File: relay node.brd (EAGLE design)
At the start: 67.8 x 40.6 mm, 25 parts, among them J1 Channels, J2 LED, J3 PROG, J4 AUX, U1 ESP-WROOM-02U, U2 MCP23018-E/SS, U5 TLV75533

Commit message: Minor changes
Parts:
- renumbered U5 to U3
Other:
- board text added: "RELAY NODE REV 1.1a"
- board text added: "RELAY NODE Rev 1.1a"
- board text removed: "SFM RELAY NODE REV 1.1a"
- board text removed: "SFM RELAY NODE Rev 1.1a"
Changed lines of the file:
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@@
 <grid distance="0.127" unitdist="mm" unit="mm" style="lines" multiple="1" display="yes" altdistance="0.0127" altunitdist="mm" altunit="mm"/>
 <layers>
-<layer number="1" name="Top" color="4" fill="1" visible="yes" active="yes"/>
+<layer number="1" name="Top" color="4" fill="1" visible="no" active="yes"/>
 <layer number="16" name="Bottom" color="1" fill="1" visible="yes" active="yes"/>
-<layer number="17" name="Pads" color="2" fill="1" visible="yes" active="yes"/>
-<layer number="18" name="Vias" color="2" fill="1" visible="yes" active="yes"/>
-<layer number="19" name="Unrouted" color="6" fill="1" visible="yes" active="yes"/>
-<layer number="20" name="Dimension" color="24" fill="1" visible="yes" active="yes"/>
-<layer number="21" name="tPlace" color="7" fill="1" visible="yes" active="yes"/>
-<layer number="22" name="bPlace" color="7" fill="1" visible="yes" active="yes"/>
-<layer number="23" name="tOrigins" color="15" fill="1" visible="yes" active="yes"/>
-<layer number="24" name="bOrigins" color="15" fill="1" visible="yes" active="yes"/>
-<layer number="25" name="tNames" color="7" fill="1" visible="yes" active="yes"/>
-<layer number="26" name="bNames" color="7" fill="1" visible="yes" active="yes"/>
+<layer number="17" name="Pads" color="2" fill="1" visible="no" active="yes"/>
+<layer number="18" name="Vias" color="2" fill="1" visible="no" active="yes"/>
+<layer number="19" name="Unrouted" color="6" fill="1" visible="no" active="yes"/>
+<layer number="20" name="Dimension" color="24" fill="1" visible="no" active="yes"/>
+<layer number="21" name="tPlace" color="7" fill="1" visible="no" active="yes"/>
+<layer number="22" name="bPlace" color="7" fill="1" visible="no" active="yes"/>
+<layer number="23" name="tOrigins" color="15" fill="1" visible="no" active="yes"/>
+<layer number="24" name="bOrigins" color="15" fill="1" visible="no" active="yes"/>
+<layer number="25" name="tNames" color="7" fill="1" visible="no" active="yes"/>
+<layer number="26" name="bNames" color="7" fill="1" visible="no" active="yes"/>
 <layer number="27" name="tValues" color="7" fill="1" visible="no" active="yes"/>
 <layer number="28" name="bValues" color="7" fill="1" visible="no" active="yes"/>
@@
 <layer number="37" name="tTest" color="7" fill="1" visible="no" active="yes"/>
 <layer number="38" name="bTest" color="7" fill="1" visible="no" active="yes"/>
-<layer number="39" name="tKeepout" color="4" fill="11" visible="yes" active="yes"/>
-<layer number="40" name="bKeepout" color="1" fill="11" visible="yes" active="yes"/>
-<layer number="41" name="tRestrict" color="4" fill="10" visible="yes" active="yes"/>
+<layer number="39" name="tKeepout" color="4" fill="11" visible="no" active="yes"/>
+<layer number="40" name="bKeepout" color="1" fill="11" visible="no" active="yes"/>
+<layer number="41" name="tRestrict" color="4" fill="10" visible="no" active="yes"/>
 <layer number="42" name="bRestrict" color="1" fill="10" visible="yes" active="yes"/>
 <layer number="43" name="vRestrict" color="2" fill="10" visible="no" active="yes"/>
@@
 <layer number="49" name="Reference" color="7" fill="1" visible="no" active="yes"/>
 <layer number="50" name="dxf" color="7" fill="1" visible="no" active="yes"/>
-<layer number="51" name="tDocu" color="7" fill="1" visible="yes" active="yes"/>
-<layer number="52" name="bDocu" color="7" fill="1" visible="yes" active="yes"/>
+<layer number="51" name="tDocu" color="7" fill="1" visible="no" active="yes"/>
+<layer number="52" name="bDocu" color="7" fill="1" visible="no" active="yes"/>
 <layer number="53" name="tGND_GNDA" color="7" fill="9" visible="no" active="no"/>
 <layer number="54" name="bGND_GNDA" color="1" fill="9" visible="no" active="no"/>
@@
 <text x="54.483" y="3.175" size="1.27" layer="25" rot="R90">GND</text>
 <text x="29.464" y="2.159" size="1.27" layer="25" rot="R180">5V</text>
-<text x="48.133" y="34.29" size="1.016" layer="25">SFM RELAY NODE
+<text x="48.133" y="34.29" size="1.016" layer="25">RELAY NODE
 Rev 1.1a</text>
-<text x="24.003" y="6.477" size="1.6764" layer="42" font="vector" rot="MR0">SFM RELAY NODE
+<text x="24.003" y="6.477" size="1.6764" layer="42" font="vector" rot="MR0">RELAY NODE
 REV 1.1a</text>
 </plain>
@@
 </autorouter>
 <elements>
-<element name="U5" library="SFM-Project" package="SOT95P280X145-5N" value="TLV75533" x="16.891" y="6.477" smashed="yes" rot="R180">
+<element name="U3" library="SFM-Project" package="SOT95P280X145-5N" value="TLV75533" x="16.891" y="6.477" smashed="yes" rot="R180">
 <attribute name="DESCRIPTION" value=" Linear Voltage Regulator IC 1 Output 500mA SOT-23-5 " x="16.891" y="6.477" size="1.778" layer="27" rot="R180" display="off"/>
 <attribute name="DIGI-KEY_PART_NUMBER" value="296-50411-1-ND" x="16.891" y="6.477" size="1.778" layer="27" rot="R180" display="off"/>
@@
 <signals>
 <signal name="GND">
-<contactref element="U5" pad="2"/>
+<contactref element="U3" pad="2"/>
 <polygon width="0.1524" layer="1" isolate="0.254" locked="yes">
 <vertex x="0.127" y="0.127"/>
@@
 </signal>
 <signal name="3.3V">
-<contactref element="U5" pad="5"/>
+<contactref element="U3" pad="5"/>
 <contactref element="R1" pad="2"/>
 <contactref element="R4" pad="2"/>
@@
 </signal>
 <signal name="N$1">
-<contactref element="U5" pad="1"/>
+<contactref element="U3" pad="1"/>
 <contactref element="D1" pad="C"/>
-<contactref element="U5" pad="3"/>
+<contactref element="U3" pad="3"/>
 <contactref element="D2" pad="C"/>
 <contactref element="C1" pad="1"/>

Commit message: Move J1 to bottom layer Add J1 to J3 connectors to BOM for quotes
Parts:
- moved J1 2.59 mm to (28.5, 6.57), flipped to the bottom, turned to 180 degrees
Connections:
- net CH1: now also J1.4; no longer J1.3
- net CH10: now also J1.11; no longer J1.12
- net CH11: now also J1.14; no longer J1.13
- net CH12: now also J1.13; no longer J1.14
- net CH13: now also J1.16; no longer J1.15
- net CH14: now also J1.15; no longer J1.16
- net CH15: now also J1.18; no longer J1.17
- net CH16: now also J1.17; no longer J1.18
- net CH2: now also J1.3; no longer J1.4
- net CH3: now also J1.6; no longer J1.5
- net CH4: now also J1.5; no longer J1.6
- net CH5: now also J1.8; no longer J1.7
- net CH6: now also J1.7; no longer J1.8
- net CH7: now also J1.10; no longer J1.9
- net CH8: now also J1.9; no longer J1.10
- net CH9: now also J1.12; no longer J1.11
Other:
- board text added: "K"
- board text added: "RELAY NODE REV 1.2a"
- board text added: "RELAY NODE Rev 1.2a"
- board text removed: "RELAY NODE REV 1.1a"
- board text removed: "RELAY NODE Rev 1.1a"

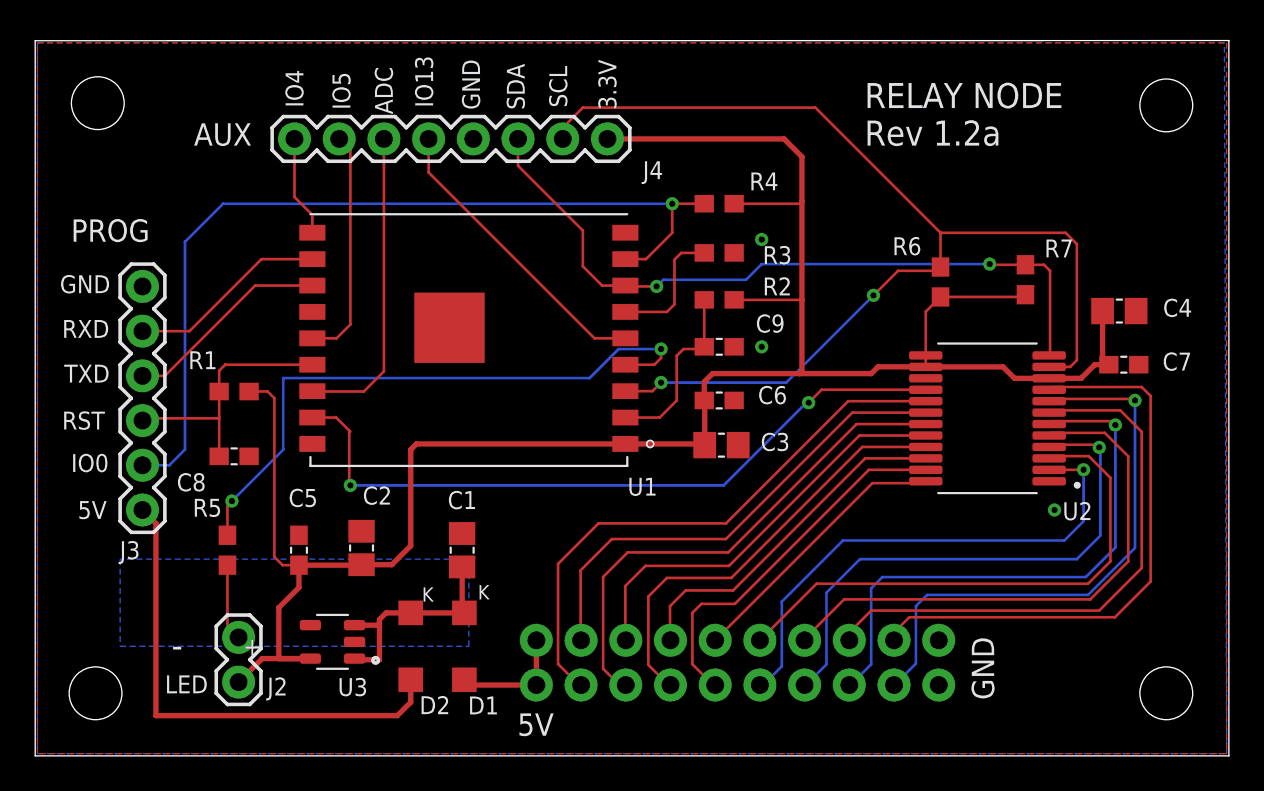
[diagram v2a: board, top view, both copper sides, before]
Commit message: Replace I/O expander to MCP23018 28-SOIC Replace BOM part numbers to match JLCPB inventory
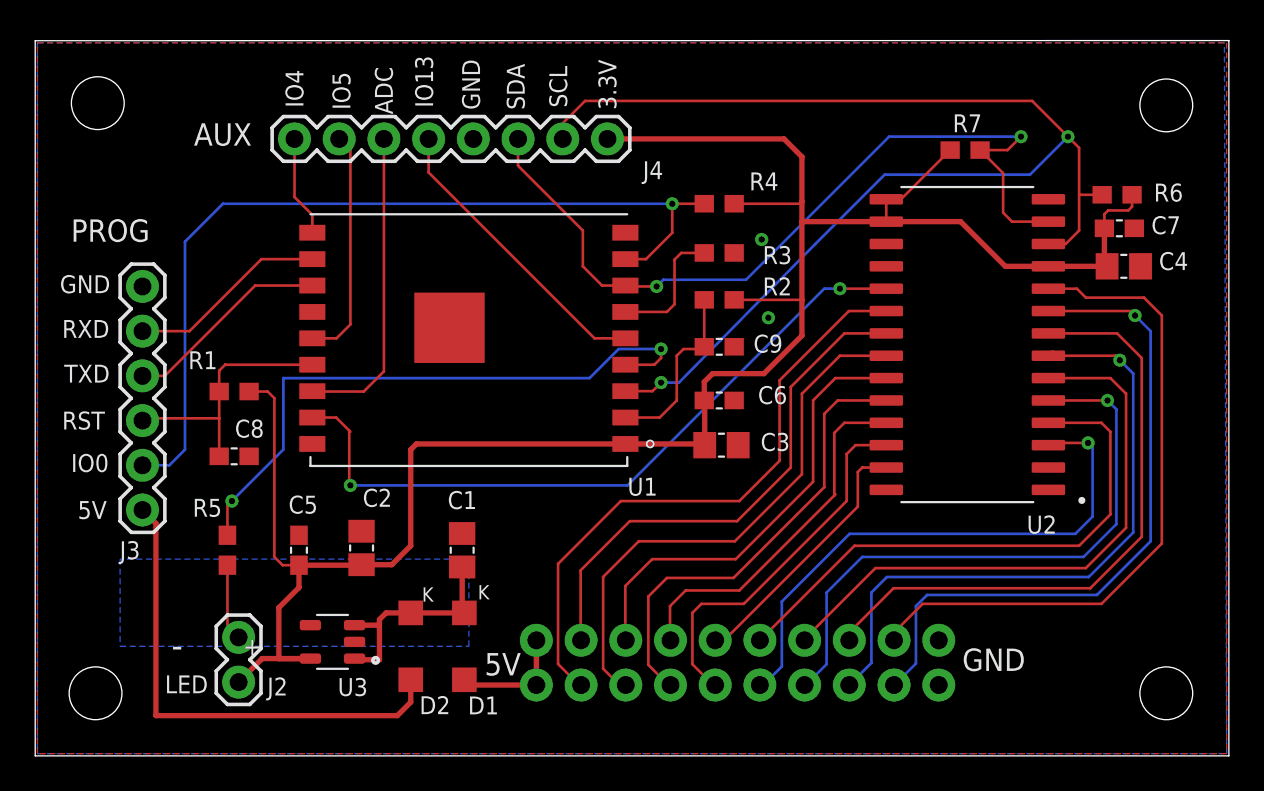
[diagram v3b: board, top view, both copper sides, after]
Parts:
- U2: value MCP23018-E/SS -> MCP23018-E/SO; device SFM-Project:SOP65P780X200-24N -> SFM-Project:SOIC127P1030X265-28N
- moved R6 11.2 mm to (61.5, 31.9), turned to 0 degrees
- moved R7 8.13 mm to (52.8, 34.4), turned to 180 degrees
- moved C7 7.75 mm to (61.6, 30.0)
- moved U2 4.34 mm to (53.0, 23.4)
- moved C4 2.55 mm to (61.8, 27.8)
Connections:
- net 3.3V: now also U2.11, U2.15, U2.16; no longer U2.10, U2.13, U2.14
- net CH1: now also U2.20; no longer U2.17
- net CH10: now also U2.4; no longer U2.3
- net CH11: now also U2.5; no longer U2.4
- net CH12: now also U2.6; no longer U2.5
- net CH13: now also U2.7; no longer U2.6
- net CH14: now also U2.8; no longer U2.7
- net CH15: now also U2.9; no longer U2.8
- net CH16: now also U2.10; no longer U2.9
- net CH2: now also U2.21; no longer U2.18
- net CH3: now also U2.22; no longer U2.19
- net CH4: now also U2.23; no longer U2.20
- net CH5: now also U2.24; no longer U2.21
- net CH6: now also U2.25; no longer U2.22
- net CH7: now also U2.26; no longer U2.23
- net CH8: now also U2.27; no longer U2.24
- net CH9: now also U2.3; no longer U2.2
- net INT: now also U2.19; no longer U2.16
- net SCL: now also U2.12; no longer U2.11
- net SDA: now also U2.13; no longer U2.12
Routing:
- net SCL: track 64.6 -> 71.1 mm
- net CH15: track 32.2 -> 38.1 mm
- net SDA: track 41.3 -> 47.2 mm
- net CH16: track 32.8 -> 38.0 mm
- net CH13: track 32.0 -> 36.7 mm
- net CH11: track 30.7 -> 34.5 mm
- net CH14: track 32.1 -> 35.3 mm
- net CH1: track 32.2 -> 34.8 mm
- net CH9: track 29.3 -> 31.6 mm
- net CH2: track 27.3 -> 29.6 mm
- net CH3: track 28.8 -> 30.9 mm
- net 3.3V: track 125.1 -> 123.1 mm
- net CH12: track 31.4 -> 33.4 mm
- net CH4: track 23.7 -> 25.5 mm
- net CH8: track 16.4 -> 15.0 mm
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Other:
- board text added: "RELAY NODE v2.1.0"
- board text removed: "RELAY NODE REV 1.2a"
- board text removed: "RELAY NODE Rev 1.2a"
